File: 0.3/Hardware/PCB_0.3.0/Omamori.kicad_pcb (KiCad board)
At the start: 2 copper layers, 25 x 35 mm, 33 parts, among them J1 Conn_01x03_Female, J2 Conn_01x07_Female, U1 BQ25570, U2 ATtiny1626, U3 TS-1233

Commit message: Small redesign
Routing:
- net GND: track 269.8 -> 271.3 mm, vias 9 -> 8
- net /Vcc_ATTiny: track 47.6 -> 48.9 mm
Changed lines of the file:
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@@
   (via (at 20.3 21.9) (size 0.8) (drill 0.4) (layers "F.Cu" "B.Cu") (net 1))
   (via (at 27.79375 28.69375) (size 0.8) (drill 0.4) (layers "F.Cu" "B.Cu") (net 1))
-  (via (at 22 24.1) (size 0.8) (drill 0.4) (layers "F.Cu" "B.Cu") (free) (net 1))
   (via (at 26.4875 36.2125) (size 0.8) (drill 0.4) (layers "F.Cu" "B.Cu") (net 1))
   (via (at 29.1 15.6) (size 0.8) (drill 0.4) (layers "F.Cu" "B.Cu") (net 1))
@@
   (segment (start 26.4875 36.2125) (end 25.2375 34.9625) (width 1) (layer "B.Cu") (net 1))
   (segment (start 23.3375 25.4375) (end 22 24.1) (width 1) (layer "B.Cu") (net 1))
-  (segment (start 22.2 17.5375) (end 22 17.7375) (width 0.5) (layer "B.Cu") (net 1))
   (segment (start 24.825 26.4625) (end 24.40625 26.04375) (width 1) (layer "B.Cu") (net 1))
   (segment (start 26.577825 32.877825) (end 27.522175 32.877825) (width 1) (layer "B.Cu") (net 1))
@@
   (segment (start 26.625 27.05) (end 26.575 27) (width 0.5) (layer "B.Cu") (net 1))
   (segment (start 29.35 22.65) (end 29.85 22.15) (width 0.25) (layer "B.Cu") (net 1))
+  (segment (start 22.2 17.5375) (end 22 17.7375) (width 1) (layer "B.Cu") (net 1))
+  (segment (start 22.2 16.1) (end 22.2 17.5375) (width 1) (layer "B.Cu") (net 1))
   (segment (start 22 17.7375) (end 20.775 17.7375) (width 0.5) (layer "B.Cu") (net 1))
   (segment (start 26.127825 32.877825) (end 24.825 31.575) (width 1) (layer "B.Cu") (net 1))
@@
   (segment (start 31.5375 21.65) (end 32.8125 21.65) (width 0.25) (layer "B.Cu") (net 6))
   (segment (start 32.3 20.3) (end 32.7625 20.3) (width 1) (layer "B.Cu") (net 6))
-  (segment (start 17.555 25.345) (end 19.9 23) (width 1) (layer "F.Cu") (net 7))
-  (segment (start 23.4375 23) (end 19.9 23) (width 1) (layer "F.Cu") (net 7))
-  (segment (start 15.2 25.345) (end 17.555 25.345) (width 1) (layer "F.Cu") (net 7))
-  (segment (start 23.8 23.3625) (end 23.4375 23) (width 1) (layer "F.Cu") (net 7))
+  (segment (start 21.1875 23.3625) (end 23.8 23.3625) (width 1) (layer "F.Cu") (net 7))
+  (segment (start 19.205 25.345) (end 19.75 24.8) (width 1) (layer "F.Cu") (net 7))
+  (segment (start 19.75 24.8) (end 21.1875 23.3625) (width 1) (layer "F.Cu") (net 7))
+  (segment (start 15.2 25.345) (end 19.205 25.345) (width 1) (layer "F.Cu") (net 7))
   (via (at 22 20.3) (size 0.8) (drill 0.4) (layers "F.Cu" "B.Cu") (net 7))
-  (via (at 19.65 23.25) (size 0.8) (drill 0.4) (layers "F.Cu" "B.Cu") (net 7))
+  (via (at 19.75 24.8) (size 0.8) (drill 0.4) (layers "F.Cu" "B.Cu") (net 7))
   (via (at 23.8 23.3625) (size 0.8) (drill 0.4) (layers "F.Cu" "B.Cu") (net 7))
   (segment (start 24 21.4625) (end 23.75 21.7125) (width 0.5) (layer "B.Cu") (net 7))
-  (segment (start 19.52548 21.8) (end 19.1 21.8) (width 0.25) (layer "B.Cu") (net 7))
   (segment (start 28.1625 21.65) (end 27.675002 21.65) (width 0.25) (layer "B.Cu") (net 7))
   (segment (start 22 21.1375) (end 22 20.3) (width 1) (layer "B.Cu") (net 7))
   (segment (start 26.849992 20.82499) (end 24.67501 20.82499) (width 0.25) (layer "B.Cu") (net 7))
+  (segment (start 19.72452 21.99904) (end 19.72452 24.77452) (width 0.25) (layer "B.Cu") (net 7))
   (segment (start 22 20.3) (end 22 19.4625) (width 1) (layer "B.Cu") (net 7))
   (segment (start 23.7425 21.705) (end 23.75 21.7125) (width 0.5) (layer "B.Cu") (net 7))
@@
   (segment (start 24.7 21.1) (end 22.0375 21.1) (width 1) (layer "B.Cu") (net 7))
   (segment (start 24.67501 20.82499) (end 24.07501 20.82499) (width 0.25) (layer "B.Cu") (net 7))
-  (segment (start 19.65 23.25) (end 19.72452 23.17548) (width 0.25) (layer "B.Cu") (net 7))
   (segment (start 23.8 22) (end 24.7 21.1) (width 1) (layer "B.Cu") (net 7))
   (segment (start 23.8 23.3625) (end 23.8 22) (width 1) (layer "B.Cu") (net 7))
+  (segment (start 19.72452 24.77452) (end 19.75 24.8) (width 0.25) (layer "B.Cu") (net 7))
   (segment (start 27.675002 21.65) (end 26.849992 20.82499) (width 0.25) (layer "B.Cu") (net 7))
-  (segment (start 19.72452 23.17548) (end 19.72452 21.99904) (width 0.25) (layer "B.Cu") (net 7))
-  (segment (start 19.72452 21.99904) (end 19.52548 21.8) (width 0.25) (layer "B.Cu") (net 7))
+  (segment (start 19.1 21.8) (end 19.52548 21.8) (width 0.25) (layer "B.Cu") (net 7))
   (segment (start 13.74904 26.79596) (end 15.2 25.345) (width 0.25) (layer "B.Cu") (net 7))
   (segment (start 13.74904 38.83404) (end 13.74904 26.79596) (width 0.25) (layer "B.Cu") (net 7))
@@
   (segment (start 22.0375 21.1) (end 22 21.1375) (width 1) (layer "B.Cu") (net 7))
   (segment (start 24.67501 20.82499) (end 24.63751 20.82499) (width 0.5) (layer "B.Cu") (net 7))
+  (segment (start 19.52548 21.8) (end 19.72452 21.99904) (width 0.25) (layer "B.Cu") (net 7))
   (segment (start 29.9 25.575) (end 29.875 25.55) (width 0.5) (layer "B.Cu") (net 8))
   (segment (start 29.875 25.60096) (end 30.62452 26.35048) (width 0.25) (layer "B.Cu") (net 8))

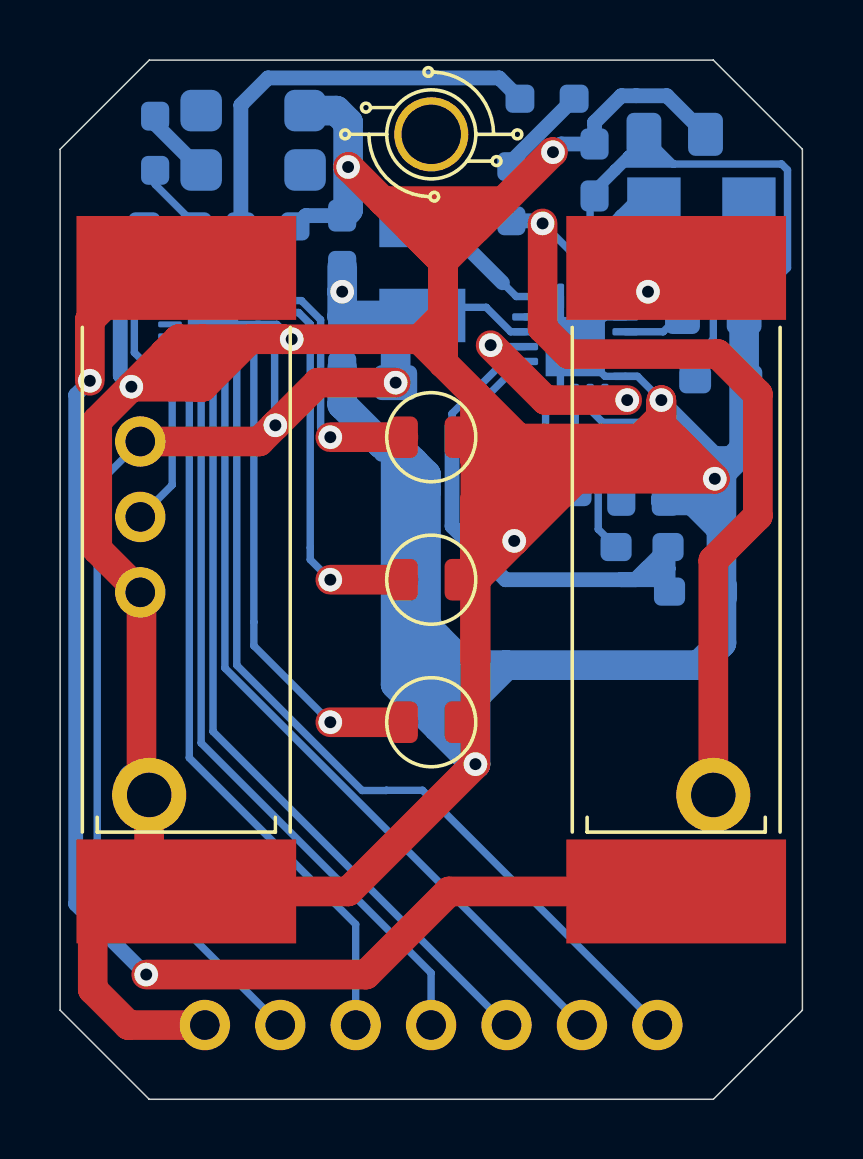
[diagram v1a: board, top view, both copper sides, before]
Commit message: Correct pcb design update for v3.
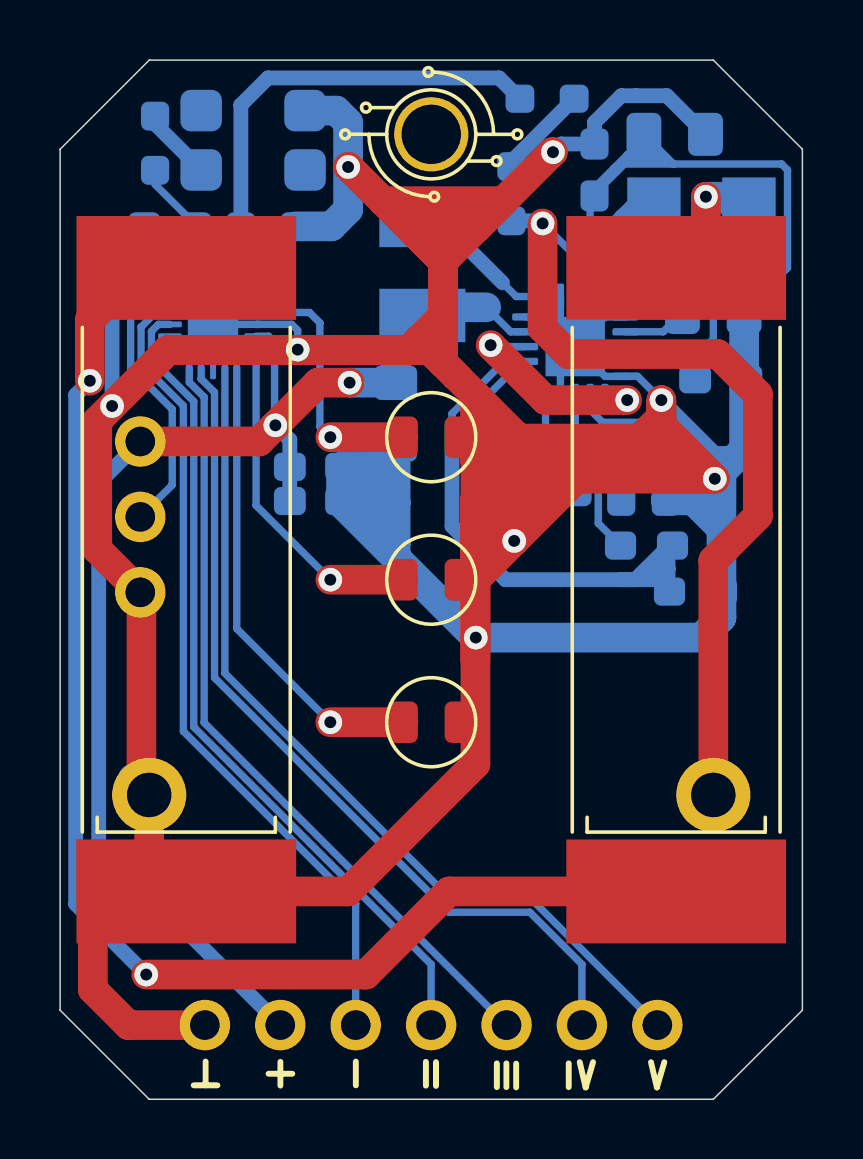
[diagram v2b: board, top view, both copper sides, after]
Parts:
- moved C_uC_Filter3 7.65 mm to (21.1, 26.2), turned to 0 degrees
- moved C_uC_Filter2 5.43 mm to (21.1, 27.4), turned to 0 degrees
- moved R_set1 0.16 mm to (32.2, 28.9)
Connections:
- J2 pad 3: /Rx -> Net-(J2-Pad3)
- J2 pad 4: /Tx -> Net-(J2-Pad4)
- J2 pad 5: Net-(J2-Pad5) -> /Rx
- J2 pad 6: Net-(J2-Pad6) -> /Tx
- U2 pad 1: /VCC_LED1 -> unconnected-(U2-Pad1)
- U2 pad 13: unconnected-(U2-Pad13) -> Net-(J2-Pad4)
- U2 pad 14: unconnected-(U2-Pad14) -> Net-(J2-Pad3)
- U2 pad 2: /VCC_LED2 -> /VCC_LED1
- U2 pad 5: /VCC_LED3 -> /VCC_LED2
- U2 pad 6: Net-(J2-Pad7) -> /VCC_LED3
- U2 pad 7: Net-(J2-Pad6) -> Net-(J2-Pad7)
- U2 pad 8: Net-(J2-Pad5) -> unconnected-(U2-Pad8)
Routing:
- net Net-(J2-Pad4): track 0.00 -> 28.0 mm
- net Net-(J2-Pad3): track 0.00 -> 27.7 mm
- net Net-(J2-Pad6): track 27.1 -> 0.00 mm
- net Net-(J2-Pad5): track 26.2 -> 0.00 mm
- net GND: track 271.3 -> 252.8 mm
- net /Tx: track 25.4 -> 29.1 mm
- net /Rx: track 24.5 -> 26.6 mm
- net /VCC_LED2: track 13.3 -> 11.3 mm
- net /Vcc_ATTiny: track 48.9 -> 47.2 mm, vias 3 -> 2
- net /Vsolar: track 9.83 -> 11.1 mm
- net /VCC_LED3: track 16.3 -> 15.7 mm
- net Net-(J2-Pad7): track 29.2 -> 29.8 mm
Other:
- board text added: "P"

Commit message: Updated to version, which got ordered on jlcpcb.
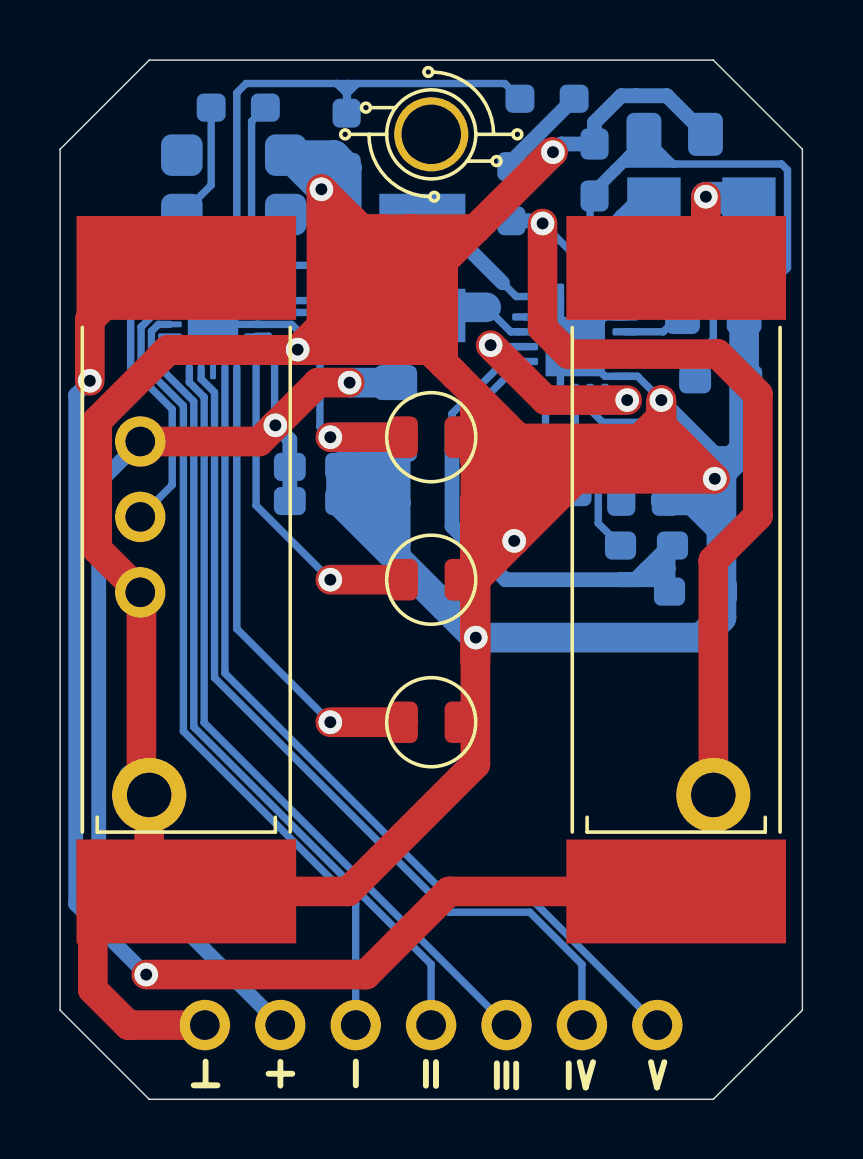
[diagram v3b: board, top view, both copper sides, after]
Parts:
- C_filter1: value 0.1uF -> 10nF
- C_super1: value 1F -> 1.5F
- R_ok1: value 3.3M -> 6.29M
- R_ok2: value 2.7M -> 3M
- R_ok3: value 3.3M -> 3.71M
- R_out1: renamed from R_set2; value 5.6M -> 8.74M
- R_out2: renamed from R_set1; value 4.3M -> 4.26M
- R_ov1: renamed from R_ov2; value 3.3M -> 4.29M
- R_ov2: renamed from R_ov1; value 6.2M -> 8.71M
- moved C_Reset1 5.97 mm to (22.1, 18.6), turned to 90 degrees
- moved R_VDIV2 3.93 mm to (22.1, 15.2), turned to -90 degrees
- moved R_Reset1 3.05 mm to (18.5, 14.1), turned to 0 degrees
- moved U3 1.63 mm to (18.4, 16.7)
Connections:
- net /Reset renamed /Interrupt
- net /Rx renamed Net-(J2-Pad5)
- net /Tx renamed Net-(J2-Pad6)
- J1 pad 2: Net-(C_Reset1-Pad1) -> Net-(J1-Pad2)
- U2 pad 1: unconnected-(U2-Pad1) -> Net-(C_Reset1-Pad1)
- U2 pad 19: Net-(C_Reset1-Pad1) -> Net-(J1-Pad2)
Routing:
- net GND: track 252.8 -> 279.4 mm, vias 8 -> 7
- net Net-(J1-Pad2): track 0.00 -> 13.1 mm
- net Net-(C_Reset1-Pad1): track 16.5 -> 11.5 mm
- net Net-(R_VDIV1_1-Pad1): track 16.1 -> 19.5 mm
- net /Interrupt: track 2.52 -> 4.01 mm
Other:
- board text added: "お 守 り"
